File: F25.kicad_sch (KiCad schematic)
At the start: 37 parts, among them J3 B2B-PH-K-S, J4 USB_C_Receptacle_USB2.0_16P, Q1 IRLML6244, SW1 RESET, SW2 BOOT, U1 MS5611-01BA, U2 MPU-6050, U4 ESP32-S3-WROOM-1-N8, U5 AP2112K-3.3

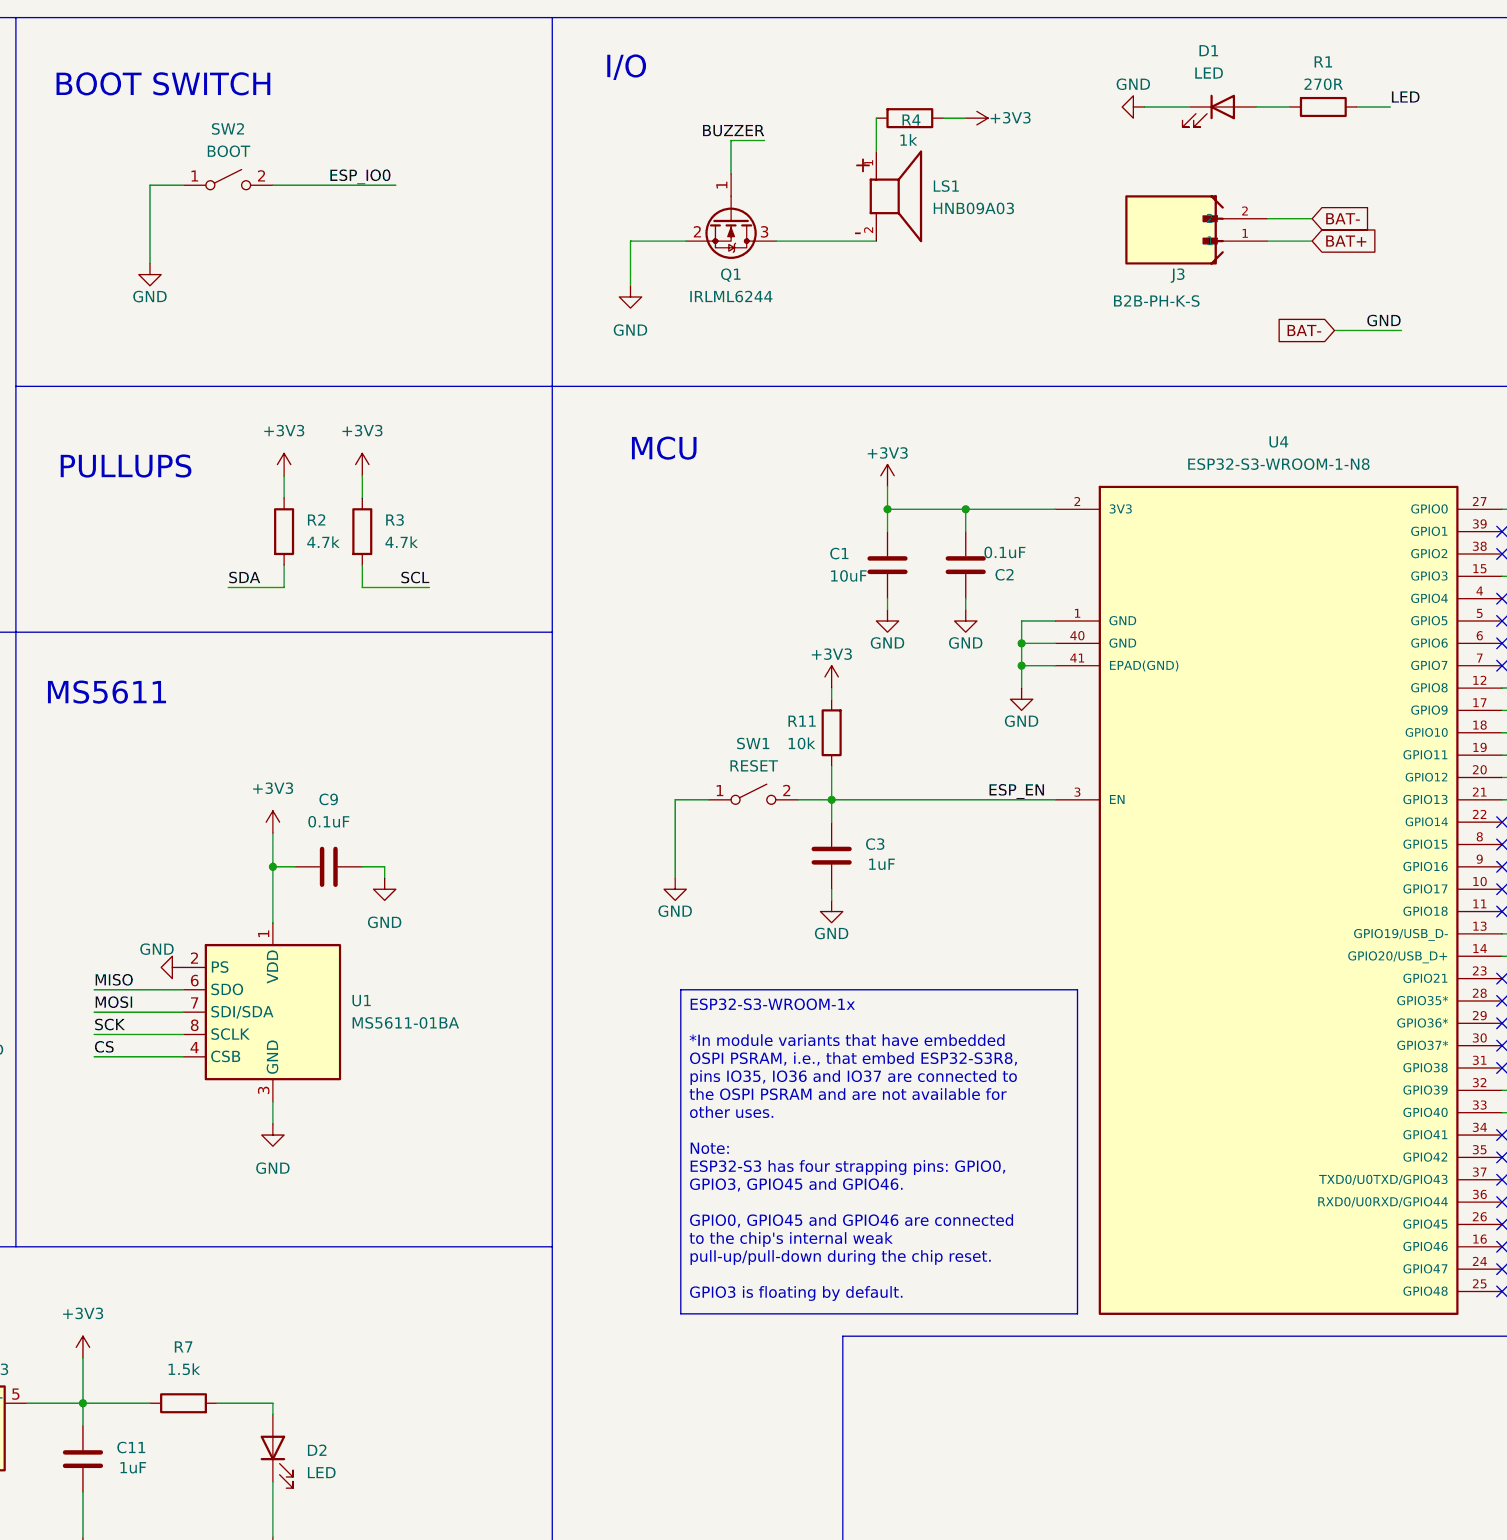
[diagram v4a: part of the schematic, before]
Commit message: LED Updates
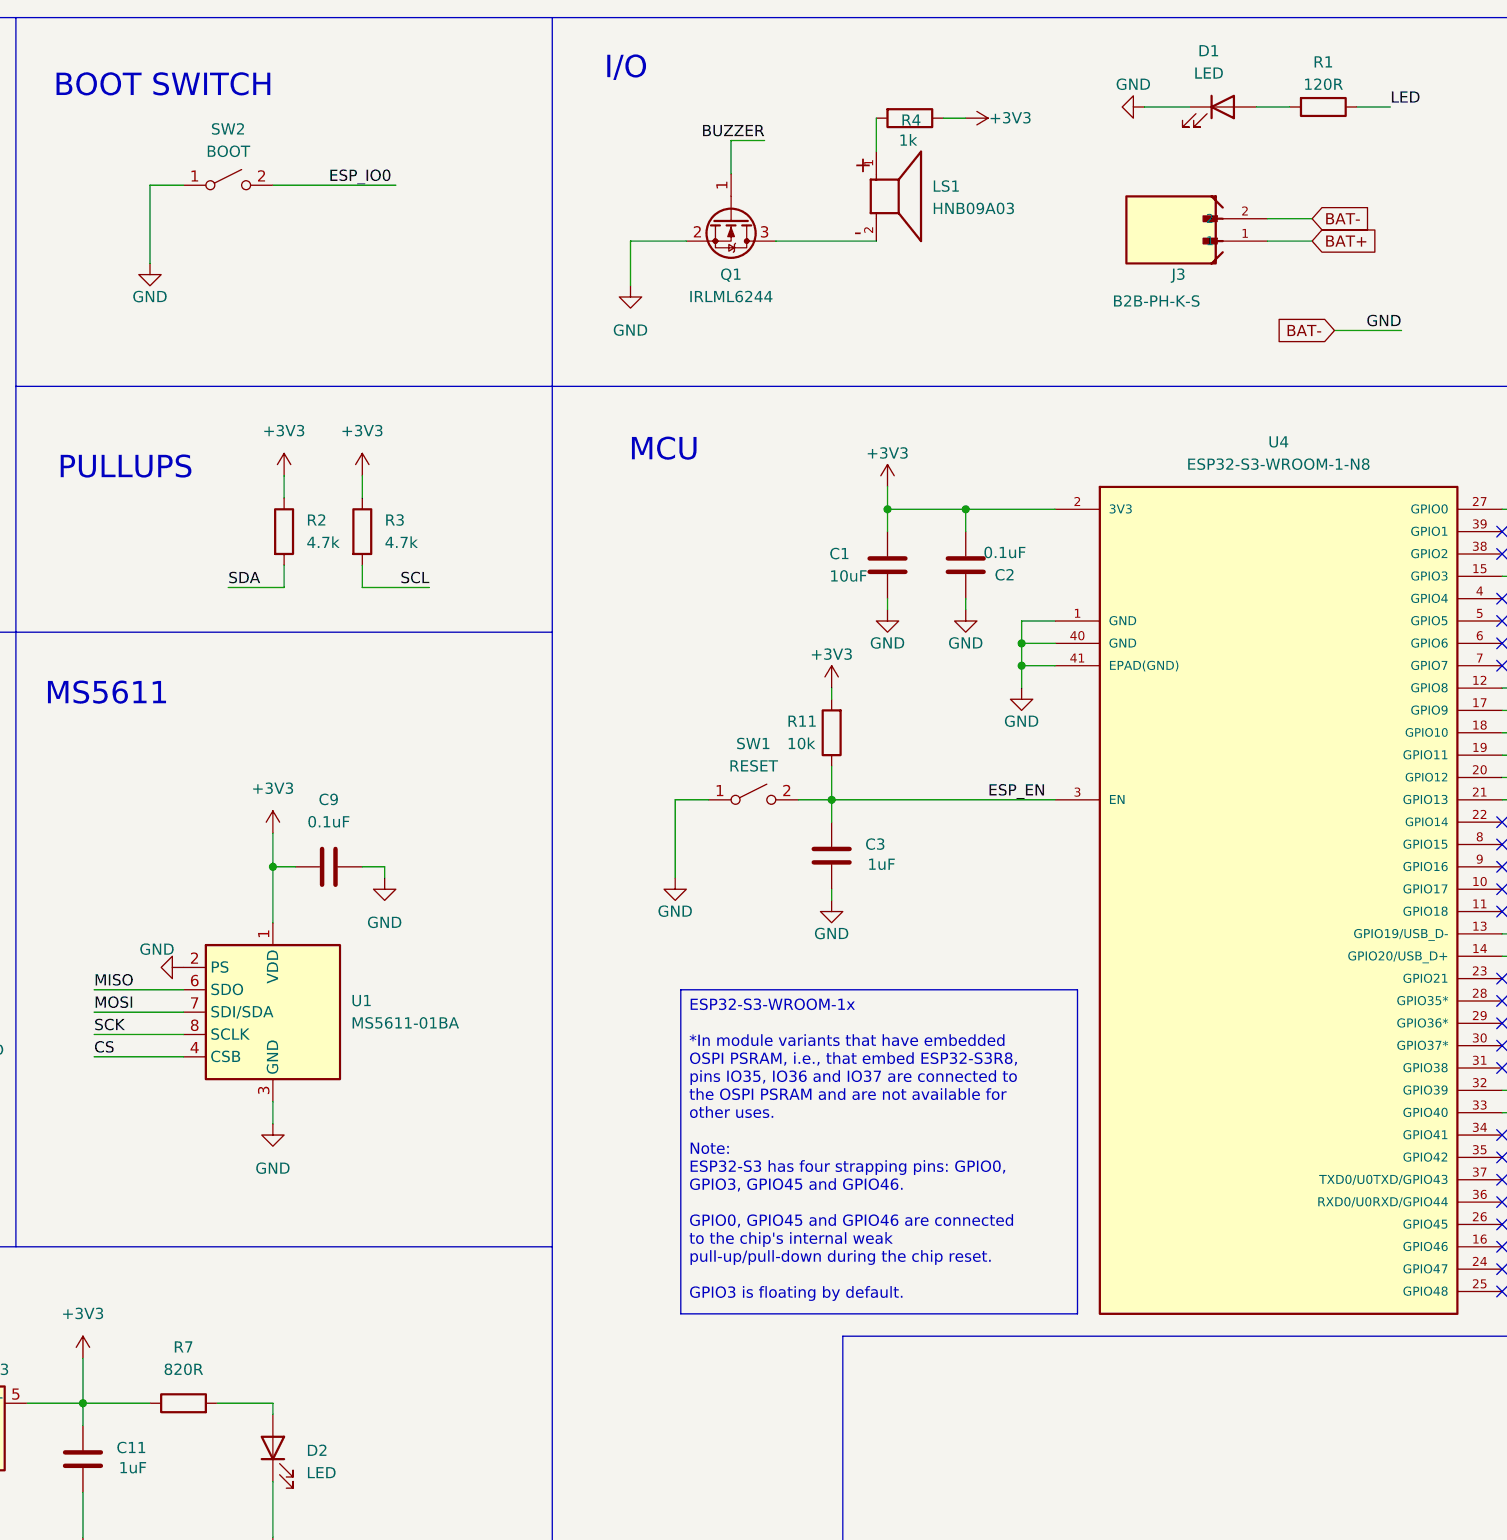
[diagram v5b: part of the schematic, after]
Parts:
- R1: value 270R -> 120R; LCSC C25099 -> C25079
- R7: value 1.5k -> 820R; LCSC C25867 -> C25135
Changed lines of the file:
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@@
 		(rev "v1.0.1")
 		(company "Metropolitan Aerospace Rocket Society")
-		(comment 1 "Author: Fawaaz Kamali Siddiqui & Anthony Dalgleish")
+		(comment 1 "Author: Anthony Dalgleish")
 	)
 	(text "I/O"
@@
 			)
 		)
-		(property "Value" "270R"
+		(property "Value" "120R"
 			(at 229.87 21.59 90)
 			(effects
@@
 			)
 		)
-		(property "LCSC" "C25099"
+		(property "LCSC" "C25079"
 			(at 229.87 24.13 0)
 			(effects
@@
 			)
 		)
-		(property "Value" "1.5k"
+		(property "Value" "820R"
 			(at 100.33 167.64 90)
 			(effects
@@
 			)
 		)
-		(property "LCSC" "C25867"
+		(property "LCSC" "C25135"
 			(at 100.33 171.45 90)
 			(effects

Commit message: Fix LED Resistors and models
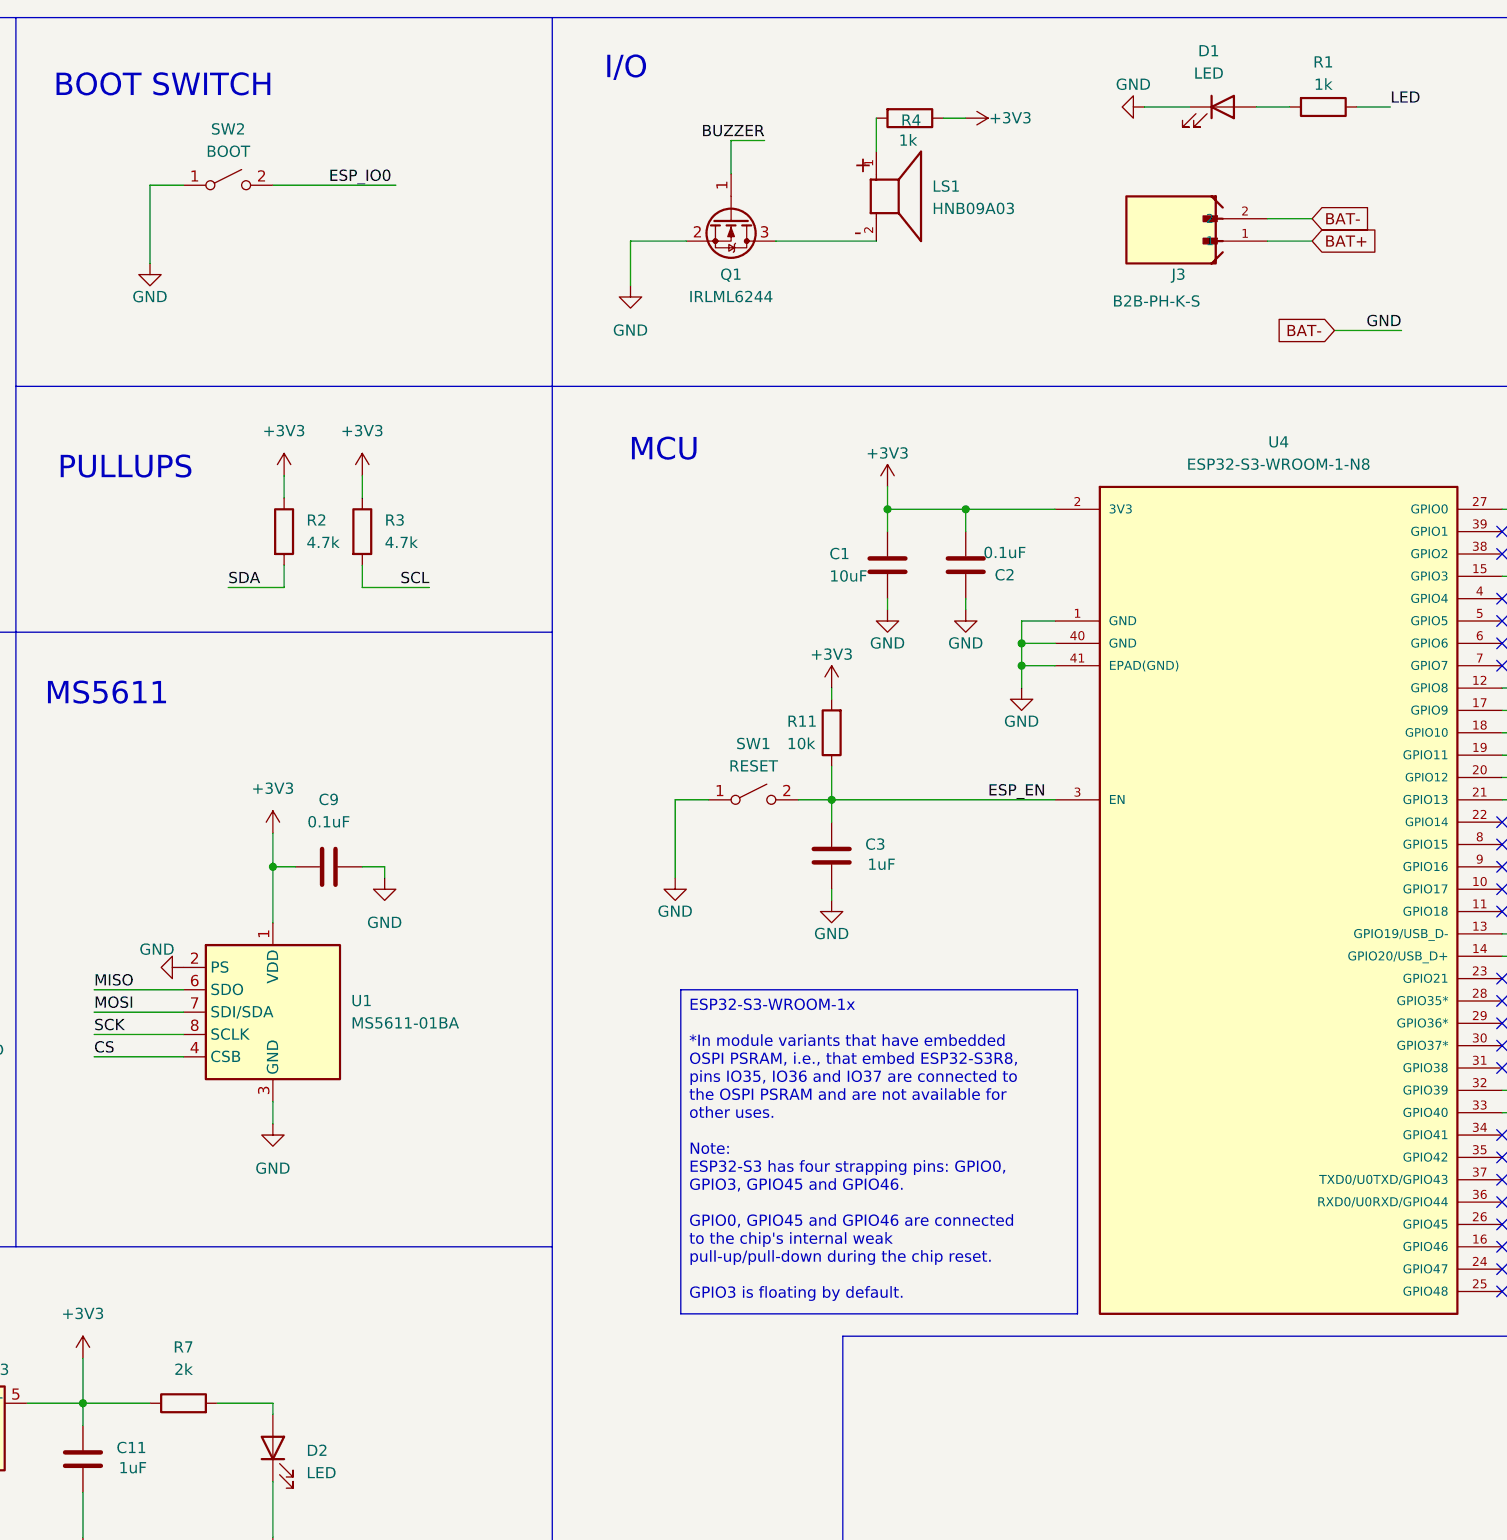
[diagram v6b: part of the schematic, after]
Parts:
- R1: value 120R -> 1k; LCSC C25079 -> C11702
- R7: value 820R -> 2k; LCSC C25135 -> C4109
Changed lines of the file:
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@@
 			)
 		)
-		(property "Value" "120R"
+		(property "Value" "1k"
 			(at 229.87 21.59 90)
 			(effects
@@
 			)
 		)
-		(property "LCSC" "C25079"
+		(property "LCSC" "C11702"
 			(at 229.87 24.13 0)
 			(effects
@@
 			)
 		)
-		(property "Value" "820R"
+		(property "Value" "2k"
 			(at 100.33 167.64 90)
 			(effects
@@
 			)
 		)
-		(property "LCSC" "C25135"
+		(property "LCSC" "C4109"
 			(at 100.33 171.45 90)
 			(effects
